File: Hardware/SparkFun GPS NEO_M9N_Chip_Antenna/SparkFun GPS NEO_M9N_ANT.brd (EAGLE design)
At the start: 40.6 x 33 mm, 93 parts, among them J13 U.FL, J2 Qwiic Right Angle, J4 Qwiic Right Angle, U1 U-BLOX_NEO-M9N, U2 3.3V

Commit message: Beings work on version with antenna
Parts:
- removed J13: U.FL, SparkFun-Connectors:U.FL
- removed U$13: (no value), SparkFun-Aesthetics:QWIIC_4MM
- removed U$25: (no value), buzzard_labels (5):JP10
- removed U$30: (no value), Labels:QWIIC-LOGO-MEDIUM
- removed U$33: (no value), SparkFun-Aesthetics:SFE_LOGO_FLAME_.1
- added U$14: (no value), SparkFun-Aesthetics:QWIIC_4MM
- added U$17: (no value), LEDs:PWR1
- added Y1: GPS_CHIP_ANTENNAW3011, SparkFun-GPS:W3011
- LED1: value Yellow -> BLUE
- U$12: device buzzard_labels:JP20 -> LEDs:PPS0
- moved U$18 11.7 mm to (38.3, 5.46), turned to 90 degrees
- moved U$55 10.6 mm to (42.3, 27.1), turned to 0 degrees
- moved U$52 8.19 mm to (35.8, 5.71), turned to 90 degrees
- moved LED2 7.10 mm to (39.4, 7.49), turned to 270 degrees
- moved LED1 4.05 mm to (37.0, 7.49), turned to 270 degrees
- moved U$12 2.39 mm to (39.9, 9.65)
- moved R1 0.71 mm to (38.1, 11.3), turned to 180 degrees
- moved R11 0.71 mm to (38.1, 9.80)
- moved J4 0.65 mm to (35.7, 15.6)
- moved R15 0.46 mm to (17.0, 29.2)
- moved J3 0.38 mm to (10.5, 26.8)
- moved D3 0.13 mm to (10.3, 24.4)
- renumbered JP1 to PPS, JP2 to PWR\, JP4 to SPI
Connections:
- net GND: now also Y1.2, Y1.3; no longer J13.1, J13.2
- net GPS_ANT1: now also Y1.1; no longer J13.FEED
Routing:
- net SCL/SCK: track 88.4 -> 74.4 mm
- net SDA/!CS: track 88.0 -> 74.3 mm, vias 4 -> 3
- net N$11: track 55.6 -> 43.3 mm
- net N$12: track 53.5 -> 41.7 mm
- net 5V: track 60.7 -> 50.1 mm
- net N$1: track 5.81 -> 2.73 mm
- net N$10: track 2.24 -> 3.93 mm
- net 3.3V: track 110.6 -> 109.8 mm
- net VCC_RF: track 2.78 -> 3.45 mm
- net RXI/MOSI: track 36.9 -> 36.3 mm

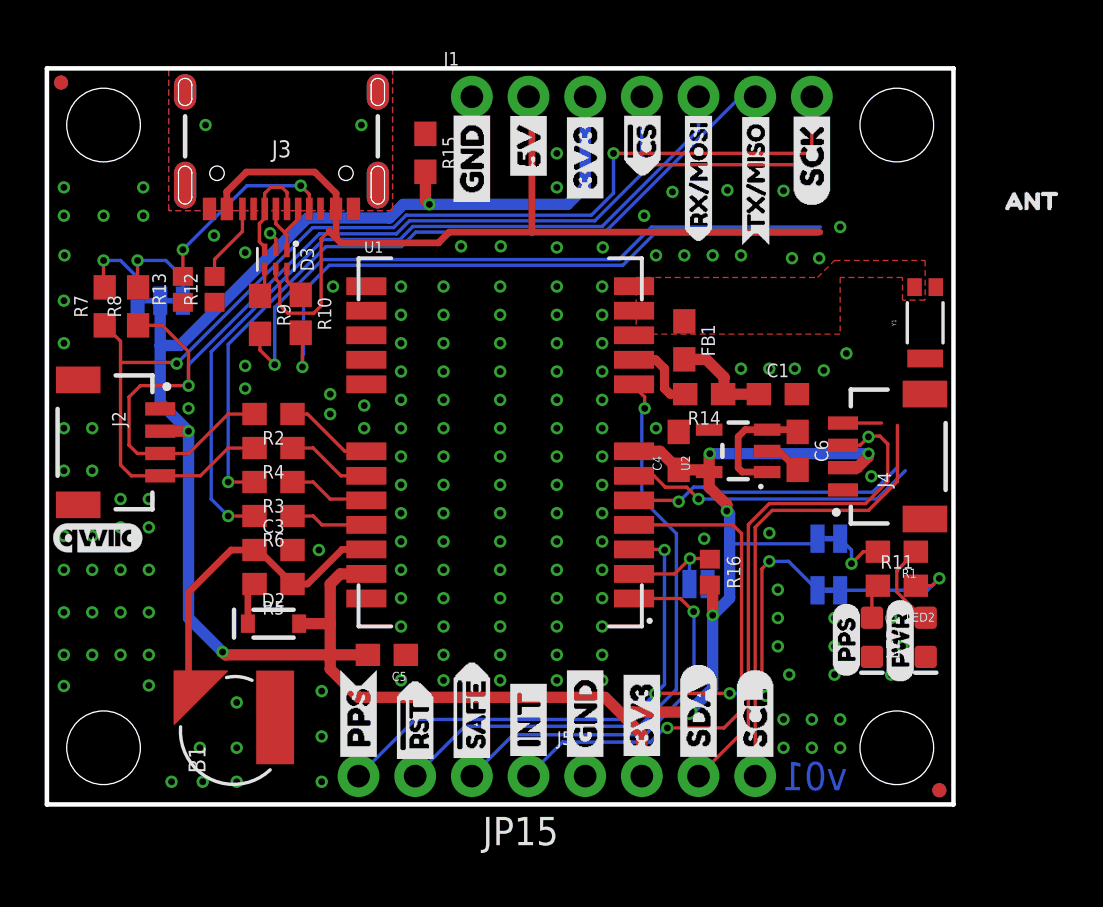
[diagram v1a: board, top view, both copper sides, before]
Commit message: Initial design for product with antenna
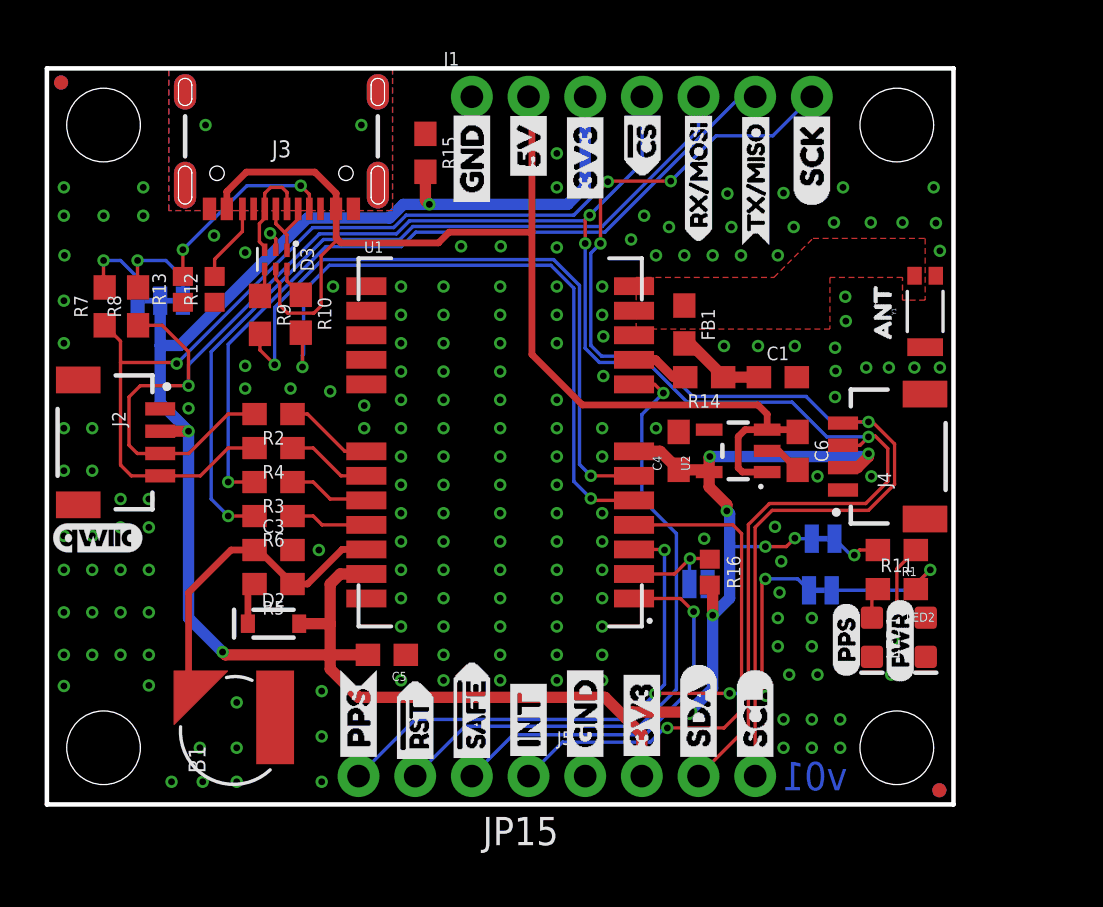
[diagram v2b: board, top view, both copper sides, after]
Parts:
- moved U$55 8.39 mm to (37.5, 20.2), turned to 90 degrees
- moved C1 0.76 mm to (32.8, 19.2)
- moved R14 0.76 mm to (29.5, 19.2)
- moved FB1 0.71 mm to (28.6, 21.5)
- moved Y1 0.51 mm to (39.4, 22.1)
- moved PPS 0.38 mm to (34.7, 9.60)
- moved PWR\ 0.25 mm to (34.8, 11.9)
- moved R11 0.15 mm to (38.1, 9.65)
- moved R1 0.08 mm to (38.1, 11.4)
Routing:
- net SCL/SCK: track 74.4 -> 93.5 mm, vias 2 -> 5
- net N$11: track 43.3 -> 29.9 mm
- net SDA/!CS: track 74.3 -> 87.3 mm, vias 3 -> 4
- net N$12: track 41.7 -> 29.7 mm
- net 5V: track 50.1 -> 54.3 mm
- net PPS: track 36.8 -> 35.4 mm
- net !RESET: track 27.9 -> 29.1 mm
- net ANT_VCC: track 4.53 -> 5.57 mm
- net VCC_RF: track 3.45 -> 2.62 mm
- net 3.3V: track 109.8 -> 109.6 mm, vias 8 -> 10
- net GND: vias 169 -> 181

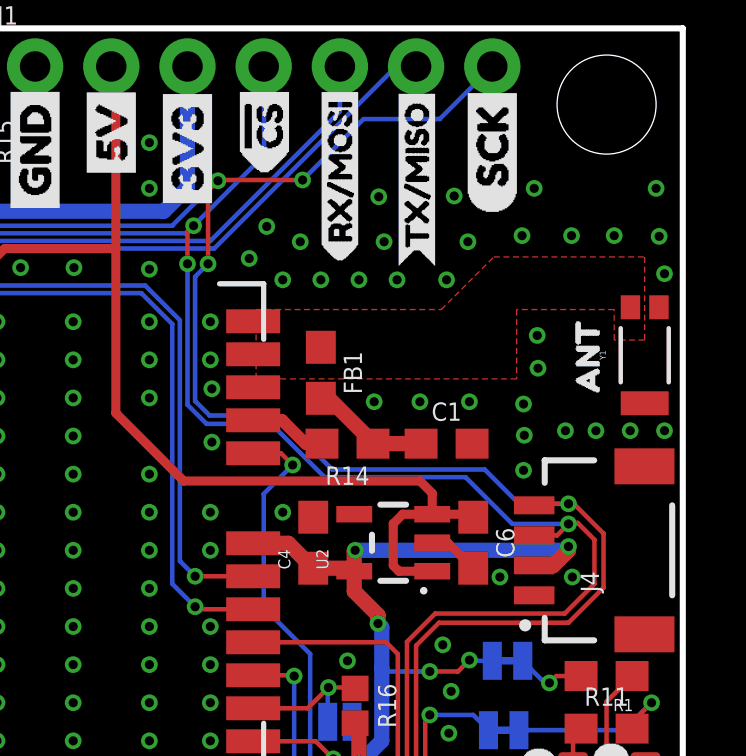
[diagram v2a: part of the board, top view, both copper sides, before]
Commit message: Adds coplanar waveguide for antenna to antenna version, adds gerbers for uFL version
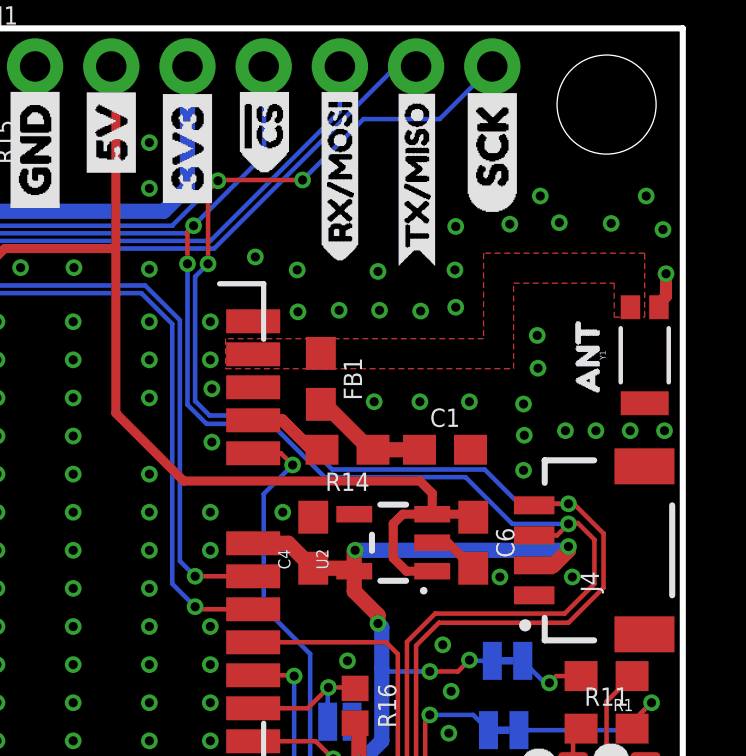
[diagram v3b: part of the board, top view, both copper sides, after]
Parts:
- moved C1 0.21 mm to (32.7, 18.9)
- moved FB1 0.20 mm to (28.6, 21.3)
- moved R14 0.20 mm to (29.5, 18.9)
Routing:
- net GND: track 2.56 -> 3.78 mm, vias 181 -> 179

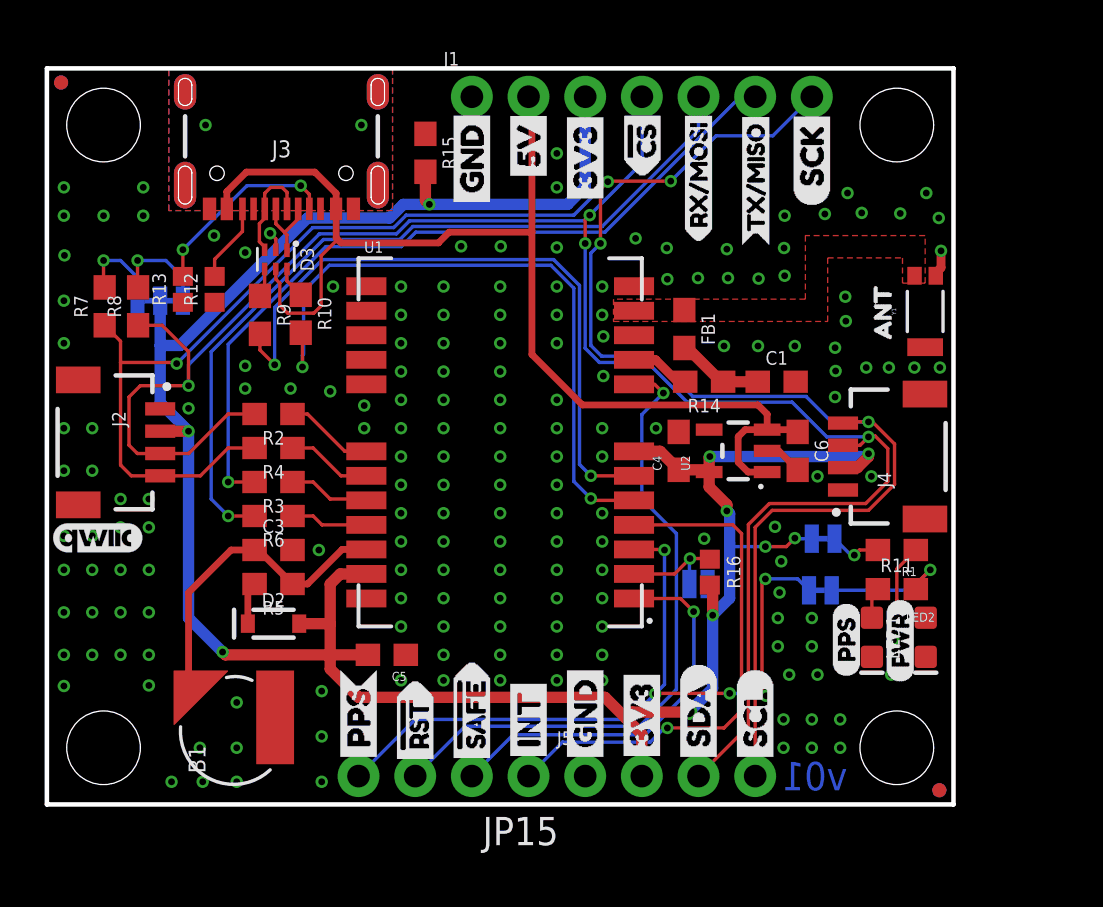
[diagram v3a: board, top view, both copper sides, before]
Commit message: Changes trace for antenna to s-bend, adds silk to battery, adds vcc range to schematic, adjusts jumper
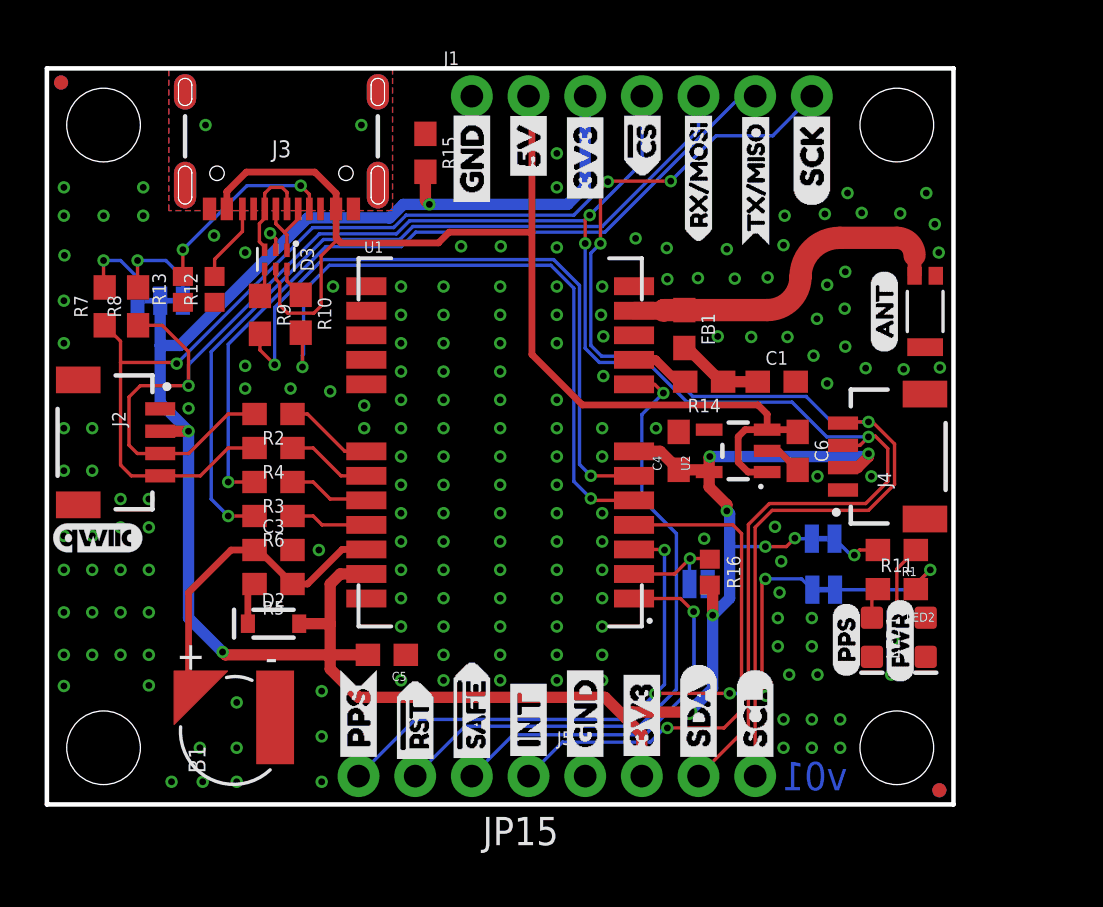
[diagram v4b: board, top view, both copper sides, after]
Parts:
- removed U$55: (no value), buzzard_labels (9):ANT0
- added U$13: (no value), ANT:ANT0
- moved PPS 0.15 mm to (34.8, 9.63)
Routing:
- net GPS_ANT1: track 0.00 -> 15.2 mm
- net GND: track 3.78 -> 2.56 mm
- removed copper zone on layer 1, net GPS_ANT1
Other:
- board text added: "+"
- board text added: "-"
